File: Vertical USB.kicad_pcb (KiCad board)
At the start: 2 copper layers, 10.7 x 9.9 mm, 3 parts, among them J1 USB_OTG, J2 Conn_01x04

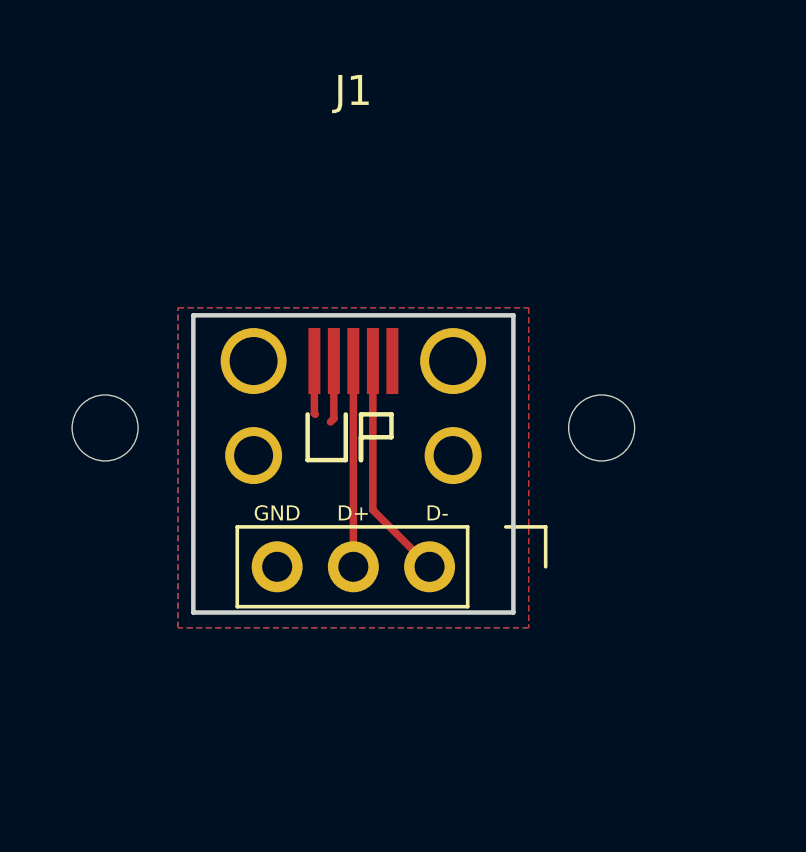
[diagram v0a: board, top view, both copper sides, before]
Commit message: 2.0
replaced header footprint with vertical USB
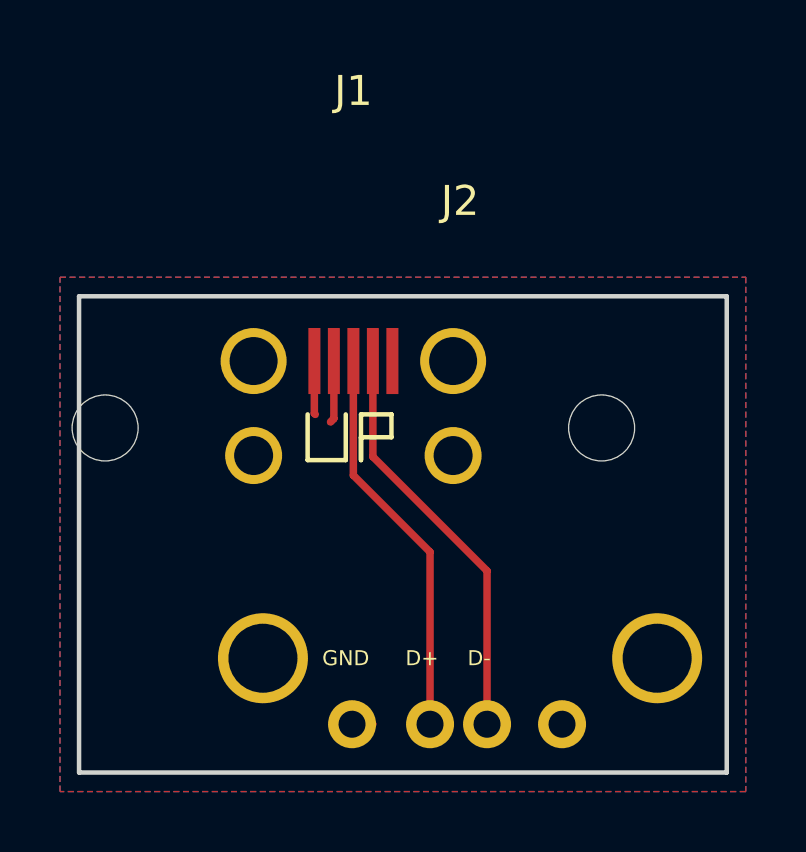
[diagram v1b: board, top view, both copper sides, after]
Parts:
- J2: footprint Pin_Headers:Pin_Header_Straight_1x04_Pitch2.54mm -> USBVERT:UJ2-AV-TH_VERTICAL_USB
- moved G*** 6.20 mm to (153.7, 115.6)
- moved J2 3.41 mm to (153.7, 118.1), turned to 180 degrees
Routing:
- net Net-(J1-Pad3): track 6.86 -> 13.2 mm
- net Net-(J1-Pad2): track 7.64 -> 13.7 mm
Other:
- board size 10.7 x 9.9 mm -> 21.6 x 15.9 mm
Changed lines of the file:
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@@
 (kicad_pcb (version 4) (host pcbnew 4.0.7)
   (general
-    (links 8)
+    (links 10)
     (no_connects 0)
-    (area 140.539 98.229 159.689 119.809619)
+    (area 140.335 98.229 163.195001 135.695)
     (thickness 1.6)
     (drawings 7)
-    (tracks 7)
+    (tracks 11)
     (zones 0)
     (modules 3)
@@
     (mod_text_size 1 1)
     (mod_text_width 0.15)
-    (pad_size 1.524 1.524)
-    (pad_drill 0.762)
+    (pad_size 3 3)
+    (pad_drill 2.3)
     (pad_to_mask_clearance 0.2)
     (aux_axis_origin 0 0)
@@
       (drillshape 0)
       (scaleselection 1)
-      (outputdirectory Gerbers/1.0/))
+      (outputdirectory Gerbers/2.0/))
   )
   (net 0 "")
@@
     (add_net "Net-(J1-Pad3)")
   )
-  (module Pin_Headers:Pin_Header_Straight_1x04_Pitch2.54mm (layer F.Cu)
-    (at 155.194 115.062 270)
-    (descr "Through hole straight pin header, 1x04, 2.54mm pitch, single row")
-    (tags "Through hole pin header THT 1x04 2.54mm single row")
-    (fp_text reference J2 (at -2.54 4.064 360) (layer F.SilkS) hide
-      (effects (font (size 1 1) (thickness 0.15)))
-    )
-    (fp_text value Conn_01x04 (at 0 9.95 270) (layer F.Fab)
-      (effects (font (size 1 1) (thickness 0.15)))
-    )
-    (fp_line (start -0.635 -1.27) (end 1.27 -1.27) (layer F.Fab) (width 0.1))
-    (fp_line (start 1.27 -1.27) (end 1.27 8.89) (layer F.Fab) (width 0.1))
-    (fp_line (start 1.27 8.89) (end -1.27 8.89) (layer F.Fab) (width 0.1))
-    (fp_line (start -1.27 8.89) (end -1.27 -0.635) (layer F.Fab) (width 0.1))
-    (fp_line (start -1.27 -0.635) (end -0.635 -1.27) (layer F.Fab) (width 0.1))
-    (fp_line (start -1.33 8.95) (end 1.33 8.95) (layer F.SilkS) (width 0.12))
-    (fp_line (start -1.33 1.27) (end -1.33 8.95) (layer F.SilkS) (width 0.12))
-    (fp_line (start 1.33 1.27) (end 1.33 8.95) (layer F.SilkS) (width 0.12))
-    (fp_line (start -1.33 1.27) (end 1.33 1.27) (layer F.SilkS) (width 0.12))
-    (fp_line (start -1.33 0) (end -1.33 -1.33) (layer F.SilkS) (width 0.12))
-    (fp_line (start -1.33 -1.33) (end 0 -1.33) (layer F.SilkS) (width 0.12))
-    (fp_line (start -1.8 -1.8) (end -1.8 9.4) (layer F.CrtYd) (width 0.05))
-    (fp_line (start -1.8 9.4) (end 1.8 9.4) (layer F.CrtYd) (width 0.05))
-    (fp_line (start 1.8 9.4) (end 1.8 -1.8) (layer F.CrtYd) (width 0.05))
-    (fp_line (start 1.8 -1.8) (end -1.8 -1.8) (layer F.CrtYd) (width 0.05))
-    (fp_text user %R (at 0 3.81 360) (layer F.Fab)
-      (effects (font (size 1 1) (thickness 0.15)))
-    )
-    (pad 2 thru_hole oval (at 0 2.54 270) (size 1.7 1.7) (drill 1) (layers *.Cu *.Mask)
-      (net 3 "Net-(J1-Pad2)"))
-    (pad 3 thru_hole oval (at 0 5.08 270) (size 1.7 1.7) (drill 1) (layers *.Cu *.Mask)
-      (net 2 "Net-(J1-Pad3)"))
-    (pad 4 thru_hole oval (at 0 7.62 270) (size 1.7 1.7) (drill 1) (layers *.Cu *.Mask)
-      (net 1 GND))
-    (model ${KISYS3DMOD}/Pin_Headers.3dshapes/Pin_Header_Straight_1x04_Pitch2.54mm.wrl
-      (at (xyz 0 0 0))
-      (scale (xyz 1 1 1))
-      (rotate (xyz 0 0 0))
-    )
-  )
   (module USBVERT:USB_MICROB_MALE_VERTICAL (layer F.Cu)
     (at 150.114 108.204 180)
@@
   )
   (module USBVERT:QR_Code (layer B.Cu)
-    (at 150.114 110.49)
+    (at 153.67 115.57)
     (fp_text reference G*** (at 0 0) (layer B.SilkS) hide
       (effects (font (thickness 0.3)) (justify mirror))
@@
       (xy -0.866885 0.324679)) (layer B.SilkS) (width 0.01))
   )
-  (gr_text GND (at 147.574 113.284) (layer F.SilkS)
+  (module USBVERT:UJ2-AV-TH_VERTICAL_USB (layer F.Cu)
+    (at 153.67 118.11 180)
+    (fp_text reference J2 (at 0 15.24 180) (layer F.SilkS)
+      (effects (font (size 1 1) (thickness 0.15)))
+    )
+    (fp_text value Conn_01x04 (at 0 -16.51 180) (layer F.Fab)
+      (effects (font (size 1 1) (thickness 0.15)))
+    )
+    (pad 1 thru_hole circle (at -3.4 -2.2 180) (size 1.6 1.6) (drill 0.9) (layers *.Cu *.Mask))
+    (pad 2 thru_hole circle (at -0.9 -2.2 180) (size 1.6 1.6) (drill 0.9) (layers *.Cu *.Mask)
+      (net 3 "Net-(J1-Pad2)"))
+    (pad 4 thru_hole circle (at 3.6 -2.2 180) (size 1.6 1.6) (drill 0.9) (layers *.Cu *.Mask)
+      (net 1 GND))
+    (pad 5 thru_hole circle (at -6.57 0 180) (size 3 3) (drill 2.3) (layers *.Cu *.Mask)
+      (net 1 GND))
+    (pad 5 thru_hole circle (at 6.57 0 180) (size 3 3) (drill 2.3) (layers *.Cu *.Mask)
+      (net 1 GND))
+    (pad 3 thru_hole circle (at 1 -2.2 180) (size 1.6 1.6) (drill 0.9) (layers *.Cu *.Mask)
+      (net 2 "Net-(J1-Pad3)"))
+  )
+  (gr_line (start 162.56 121.92) (end 162.56 106.045) (angle 90) (layer Edge.Cuts) (width 0.15))
+  (gr_line (start 140.97 121.92) (end 162.56 121.92) (angle 90) (layer Edge.Cuts) (width 0.15))
+  (gr_line (start 140.97 106.045) (end 140.97 121.92) (angle 90) (layer Edge.Cuts) (width 0.15))
+  (gr_line (start 162.56 106.045) (end 140.97 106.045) (angle 90) (layer Edge.Cuts) (width 0.15))
+  (gr_text GND (at 149.86 118.11) (layer F.SilkS)
     (effects (font (size 0.5 0.5) (thickness 0.125)))
   )
-  (gr_text D+ (at 150.114 113.284) (layer F.SilkS)
+  (gr_text D+ (at 152.4 118.11) (layer F.SilkS)
     (effects (font (size 0.5 0.5) (thickness 0.125)))
   )
-  (gr_text D- (at 152.908 113.284) (layer F.SilkS)
+  (gr_text D- (at 154.305 118.11) (layer F.SilkS)
     (effects (font (size 0.5 0.5) (thickness 0.125)))
   )
-  (gr_line (start 155.448 106.68) (end 155.448 116.586) (angle 90) (layer Edge.Cuts) (width 0.15))
-  (gr_line (start 144.78 106.68) (end 155.448 106.68) (angle 90) (layer Edge.Cuts) (width 0.15))
-  (gr_line (start 144.78 116.586) (end 144.78 106.68) (angle 90) (layer Edge.Cuts) (width 0.15))
-  (gr_line (start 155.448 116.586) (end 144.78 116.586) (angle 90) (layer Edge.Cuts) (width 0.15))
   (segment (start 149.464 108.204) (end 149.464 110.124) (width 0.25) (layer F.Cu) (net 1))
   (segment (start 149.464 110.124) (end 149.352 110.236) (width 0.25) (layer F.Cu) (net 1))
   (segment (start 148.814 108.204) (end 148.814 109.952) (width 0.25) (layer F.Cu) (net 1))
   (segment (start 148.814 109.952) (end 148.844 109.982) (width 0.25) (layer F.Cu) (net 1))
-  (segment (start 150.114 108.204) (end 150.114 115.062) (width 0.25) (layer F.Cu) (net 2))
-  (segment (start 150.764 108.204) (end 150.764 113.172) (width 0.25) (layer F.Cu) (net 3))
-  (segment (start 150.764 113.172) (end 152.654 115.062) (width 0.25) (layer F.Cu) (net 3))
+  (segment (start 150.764 120.306) (end 150.76 120.31) (width 0.25) (layer F.Cu) (net 1))
+  (segment (start 150.114 108.204) (end 150.114 112.014) (width 0.25) (layer F.Cu) (net 2))
+  (segment (start 152.67 114.57) (end 152.67 120.31) (width 0.25) (layer F.Cu) (net 2))
+  (segment (start 150.114 112.014) (end 152.67 114.57) (width 0.25) (layer F.Cu) (net 2))
+  (segment (start 150.764 108.204) (end 150.764 111.394) (width 0.25) (layer F.Cu) (net 3))
+  (segment (start 154.57 115.2) (end 154.57 120.31) (width 0.25) (layer F.Cu) (net 3))
+  (segment (start 150.764 111.394) (end 154.57 115.2) (width 0.25) (layer F.Cu) (net 3))
   (zone (net 1) (net_name GND) (layer F.Cu) (hatch edge 0.508)
     (connect_pads (clearance 0.508))
@@
     (polygon
       (pts
-        (xy 155.956 117.094) (xy 144.272 117.094) (xy 144.272 106.426) (xy 155.956 106.426)
+        (xy 163.195 122.555) (xy 140.335 122.555) (xy 140.335 105.41) (xy 163.195 105.41)
       )
     )
@@
     (polygon
       (pts
-        (xy 155.956 117.094) (xy 144.272 117.094) (xy 144.272 106.426) (xy 155.956 106.426)
+        (xy 163.195 122.555) (xy 140.335 122.555) (xy 140.335 105.41) (xy 163.195 105.41)
       )
     )
